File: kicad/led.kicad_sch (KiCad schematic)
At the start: 2 parts

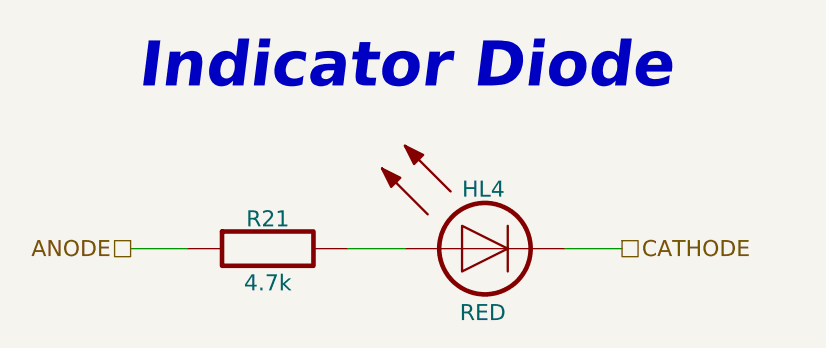
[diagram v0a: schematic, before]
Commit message: Reannotate schematic; Fix 5032 crystal footprint field; Update PCB with 5032 crystal
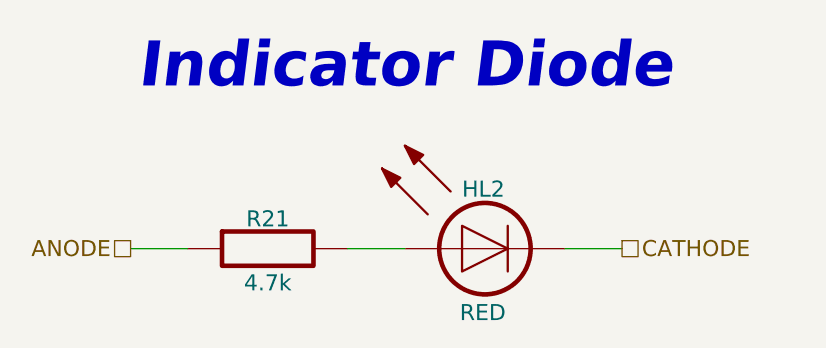
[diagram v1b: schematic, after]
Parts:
- renumbered HL4 to HL2
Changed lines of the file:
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@@
   (symbol (lib_id "Diodes:HL_LED") (at 165.354 100.076 0) (unit 1)
     (in_bom yes) (on_board yes)
-    (property "Reference" "HL4" (id 0) (at 162.814 93.472 0)
+    (property "Reference" "HL2" (id 0) (at 162.814 93.472 0)
       (effects (font (size 1.778 1.778)) (justify left))
     )

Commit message: Add voltage value to caps, update BOM, SCH, ASM
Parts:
- R21: Case/Package 0000 -> 0603; Tolerance ±% -> ±5%
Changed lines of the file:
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@@
       (effects (font (size 1.778 1.778)))
     )
-    (property "Case/Package" "0000" (id 5) (at 141.224 106.426 0)
+    (property "Case/Package" "0603" (id 5) (at 141.224 106.426 0)
       (effects (font (size 1.27 1.27)) hide)
     )
@@
       (effects (font (size 1.27 1.27)) hide)
     )
-    (property "Tolerance" "±%" (id 7) (at 141.224 109.728 0)
+    (property "Tolerance" "±5%" (id 7) (at 141.224 109.728 0)
       (effects (font (size 1.27 1.27)) hide)
     )
+    (property "Part Number" "" (id 8) (at 141.224 100.076 0))
     (pin "1")
     (pin "2")

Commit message: Add wiring diagram; Add work ours (stage 2); refactor folders
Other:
- title: (none) -> RadioSens v1
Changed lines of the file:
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@@
 (kicad_sch (version 20211123) (generator eeschema)
   (paper "A4")
+  (title_block
+    (title "RadioSens v1")
+    (comment 2 "Electrical Circuit")
+  )
   (wire (pts (xy 150.114 100.076) (xy 156.464 100.076))
     (stroke (width 0) (type default) (color 0 0 0 0))
